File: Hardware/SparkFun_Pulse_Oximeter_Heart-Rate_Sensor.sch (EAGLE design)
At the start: 33 parts, among them U1 MAX30101EFD+T, U2 MAX32664GWEA+T, U3 1.8V/100mA, Y1 32.768kHz

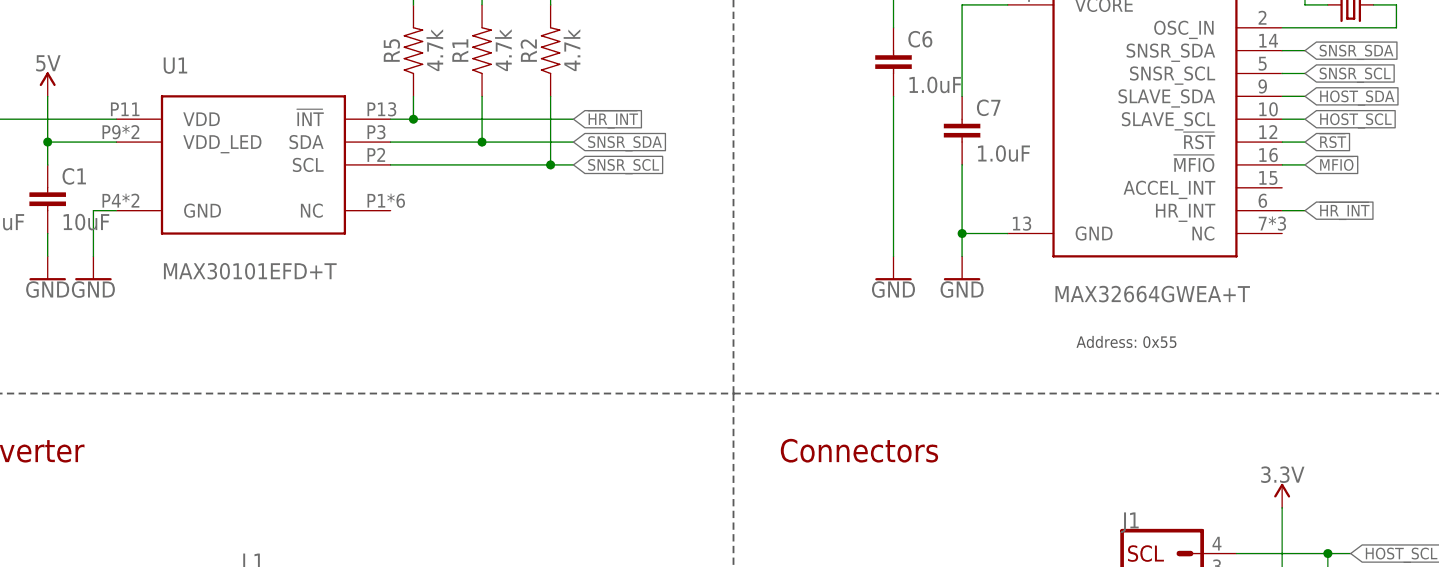
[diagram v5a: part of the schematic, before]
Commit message: Pushes temp lib to SparkFun Eagle Libraries and replaces parts in design with those parts
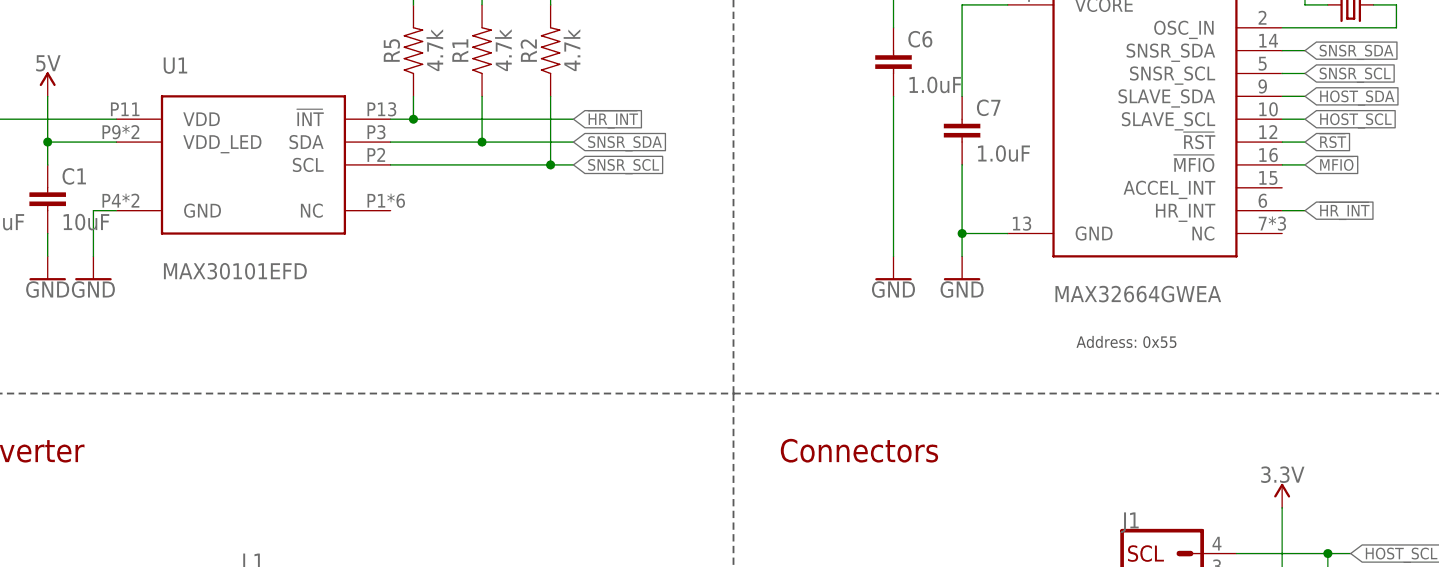
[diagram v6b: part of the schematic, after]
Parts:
- U1: value MAX30101EFD+T -> MAX30101EFD; device temp:MAX30101EFD+T -> SparkFun-IC-Special-Function:MAX30101EFD
- U2: value MAX32664GWEA+T -> MAX32664GWEA; device temp:MAX32664GWEA+T -> SparkFun-IC-Special-Function:MAX32664GWEA
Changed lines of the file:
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@@
 <part name="U3" library="SparkFun-IC-Power" deviceset="V_REG_SP6214" device="-1.8V" value="1.8V/100mA"/>
 <part name="U$2" library="SparkFun-IC-Power" deviceset="PAM2401" device="" value="PAM2401"/>
-<part name="U1" library="temp" deviceset="MAX30101EFD+T" device=""/>
-<part name="U2" library="temp" deviceset="MAX32664GWEA+T" device=""/>
+<part name="U1" library="SparkFun-IC-Special-Function" deviceset="MAX30101EFD" device=""/>
+<part name="U2" library="SparkFun-IC-Special-Function" deviceset="MAX32664GWEA" device=""/>
 <part name="R1" library="SparkFun-Resistors" deviceset="4.7KOHM" device="-0603-1/10W-1%" value="4.7k"/>
 <part name="R2" library="SparkFun-Resistors" deviceset="4.7KOHM" device="-0603-1/10W-1%" value="4.7k"/>

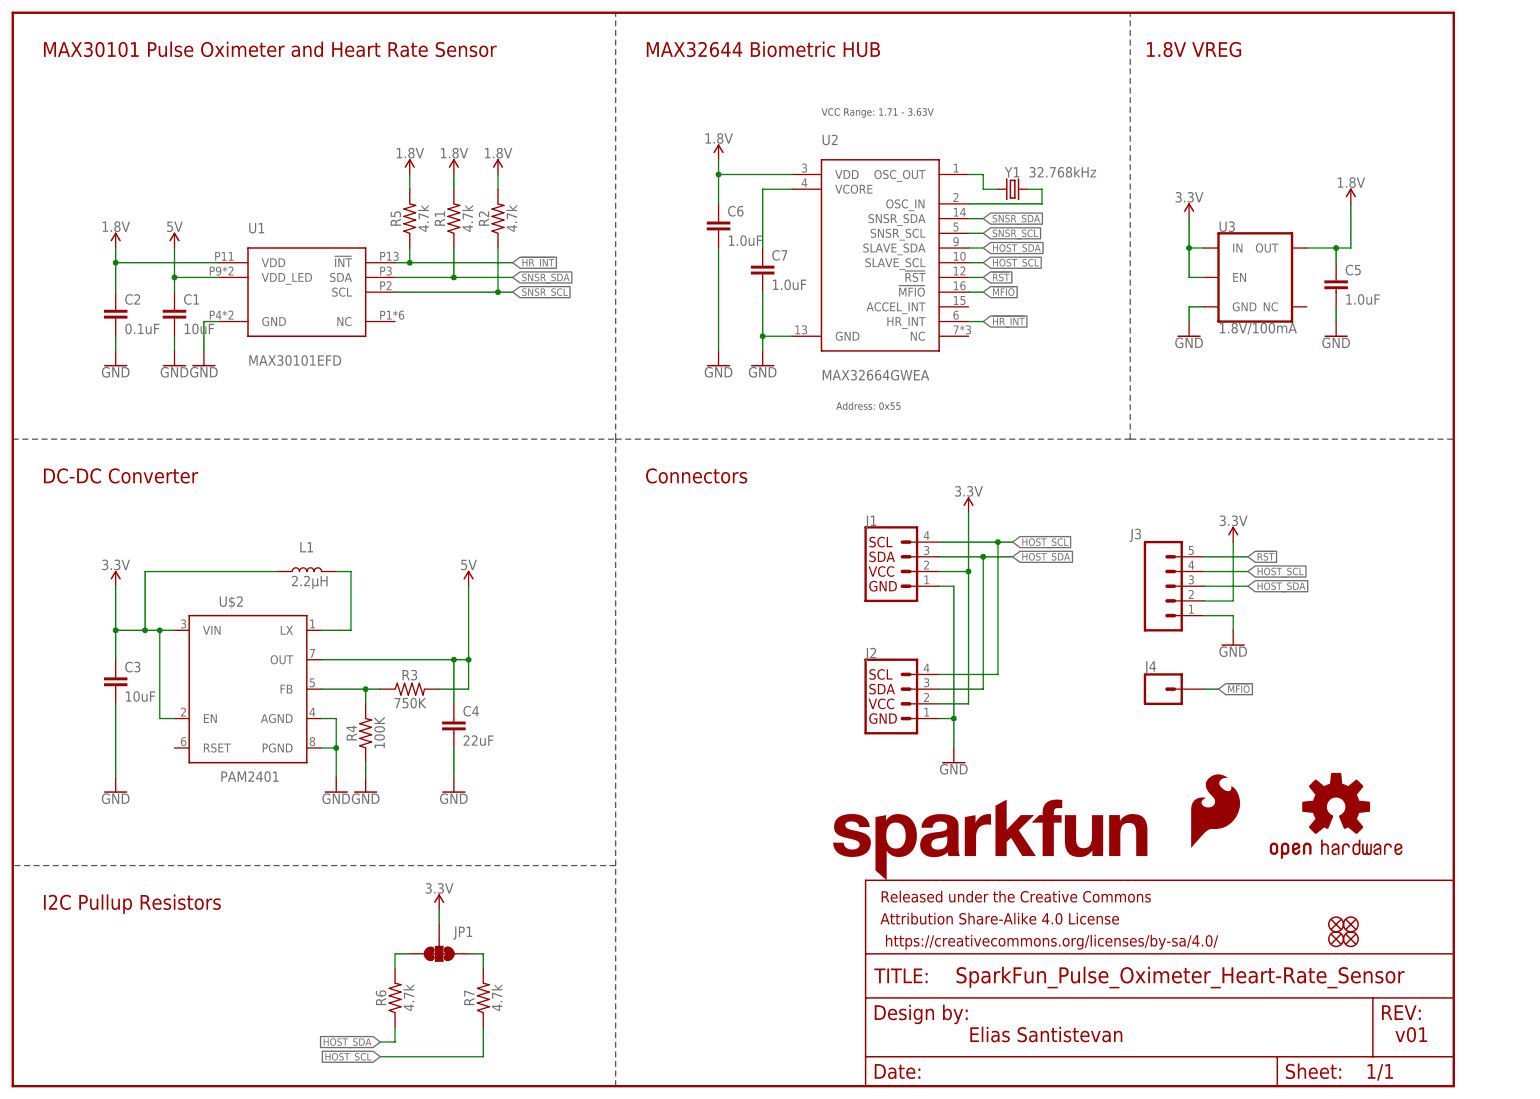
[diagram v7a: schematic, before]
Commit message: Adds dimensions and special ordering instructions, adds text to MAX30101 that lists voltage ranges and I2C addresses
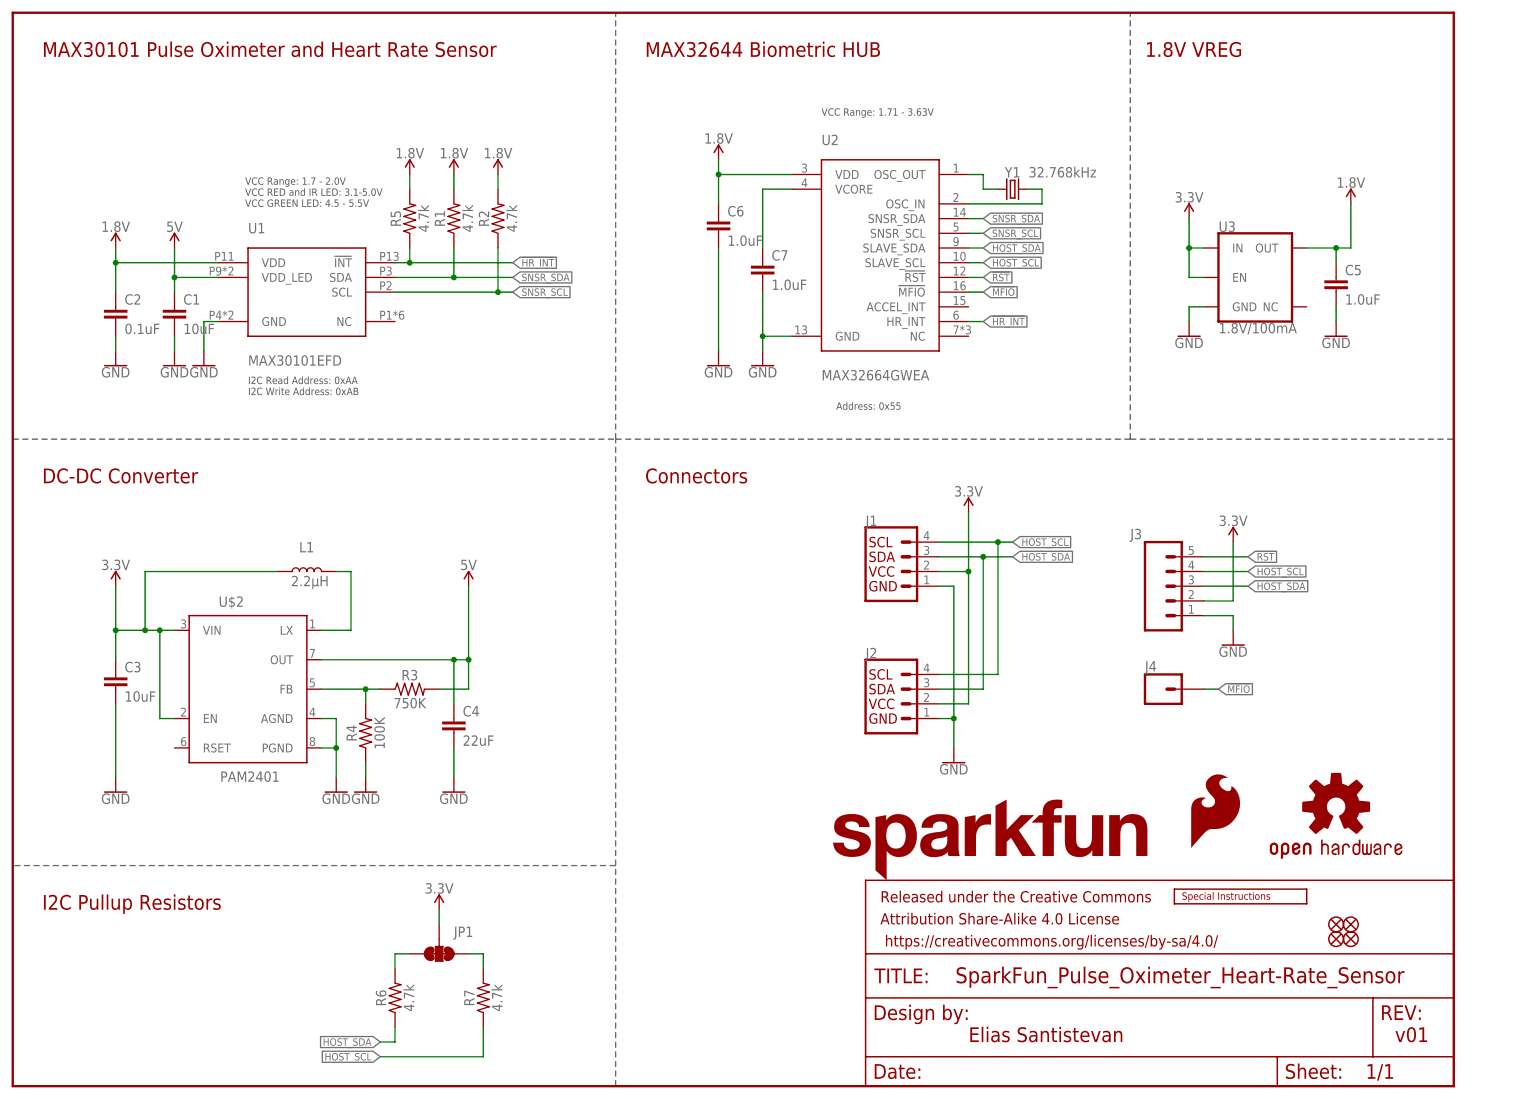
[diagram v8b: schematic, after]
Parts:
- added LOGO4: SPECIAL_INSTRUCTIONS-ORDERING, SparkFun-Aesthetics:SPECIAL_INSTRUCTIONS-ORDERING
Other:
- note added: "I2C Read Address: 0xAA I2C Write Address: 0xAB"
- note added: "VCC Range: 1.7 - 2.0V VCC RED and IR LED: 3.1-5.0V VCC GREEN LED: 4.5 - 5.5V"
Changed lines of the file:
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@@
 <part name="FD3" library="SparkFun-Aesthetics" deviceset="FIDUCIAL" device="UFIDUCIAL"/>
 <part name="FD4" library="SparkFun-Aesthetics" deviceset="FIDUCIAL" device="UFIDUCIAL"/>
+<part name="LOGO4" library="SparkFun-Aesthetics" deviceset="SPECIAL_INSTRUCTIONS" device="-ORDERING"/>
 </parts>
 <sheets>
@@
 <text x="109.22" y="104.14" size="2.54" layer="94" font="vector">Connectors</text>
 <text x="5.08" y="30.48" size="2.54" layer="94" font="vector">I2C Pullup Resistors</text>
+<text x="40.132" y="151.892" size="1.27" layer="97" font="vector">VCC Range: 1.7 - 2.0V
+VCC RED and IR LED: 3.1-5.0V
+VCC GREEN LED: 4.5 - 5.5V</text>
+<text x="40.64" y="119.38" size="1.27" layer="97" font="vector">I2C Read Address: 0xAA
+I2C Write Address: 0xAB</text>
 </plain>
 <instances>
@@
 <instance part="FD3" gate="G$1" x="231.14" y="27.94" smashed="yes"/>
 <instance part="FD4" gate="G$1" x="231.14" y="25.4" smashed="yes"/>
+<instance part="LOGO4" gate="G$1" x="200.66" y="31.496" smashed="yes"/>
 </instances>
 <busses>
@@
 </schematic>
 </drawing>
+<compatibility>
+<note version="6.3" minversion="6.2.2" severity="warning">
+Since Version 6.2.2 text objects can contain more than one line,
+which will not be processed correctly with this version.
+</note>
+</compatibility>
 </eagle>
